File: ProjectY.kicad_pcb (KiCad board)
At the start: 4 copper layers, 100 x 85 mm, 238 parts, among them J15 009155002852006, J16 009155002852006, J17 Out, J2 Conn_ARM_JTAG_SWD_10, J3 9V, J5 IN_R, J6 IN_L, J7 Out, J9 USB_C_Receptacle_USB2.0_14P, Q2 AO3401A, U1 W9825G6KH-6, U11 RT8293B, U12 USBLC6-2P6, U13 LM74700, U14 OPA1678, U2 W25Q128JVS, U201 OPA1678, U202 OPA1678, U203 OPA1678, U204 OPA1678, U205 TAC5242, U206 OPA1678, U3 FM24CL64B, U4 TPS7A39, U5 TL431DBZ, U6 MIMXRT1176CVM8A, U8 TLV77325PDBVR, U9 TL431DBZ, Y1 ASDLJ-E-24.576MHZ-L-R-T, Y3 SG-5032CAN 24MHz

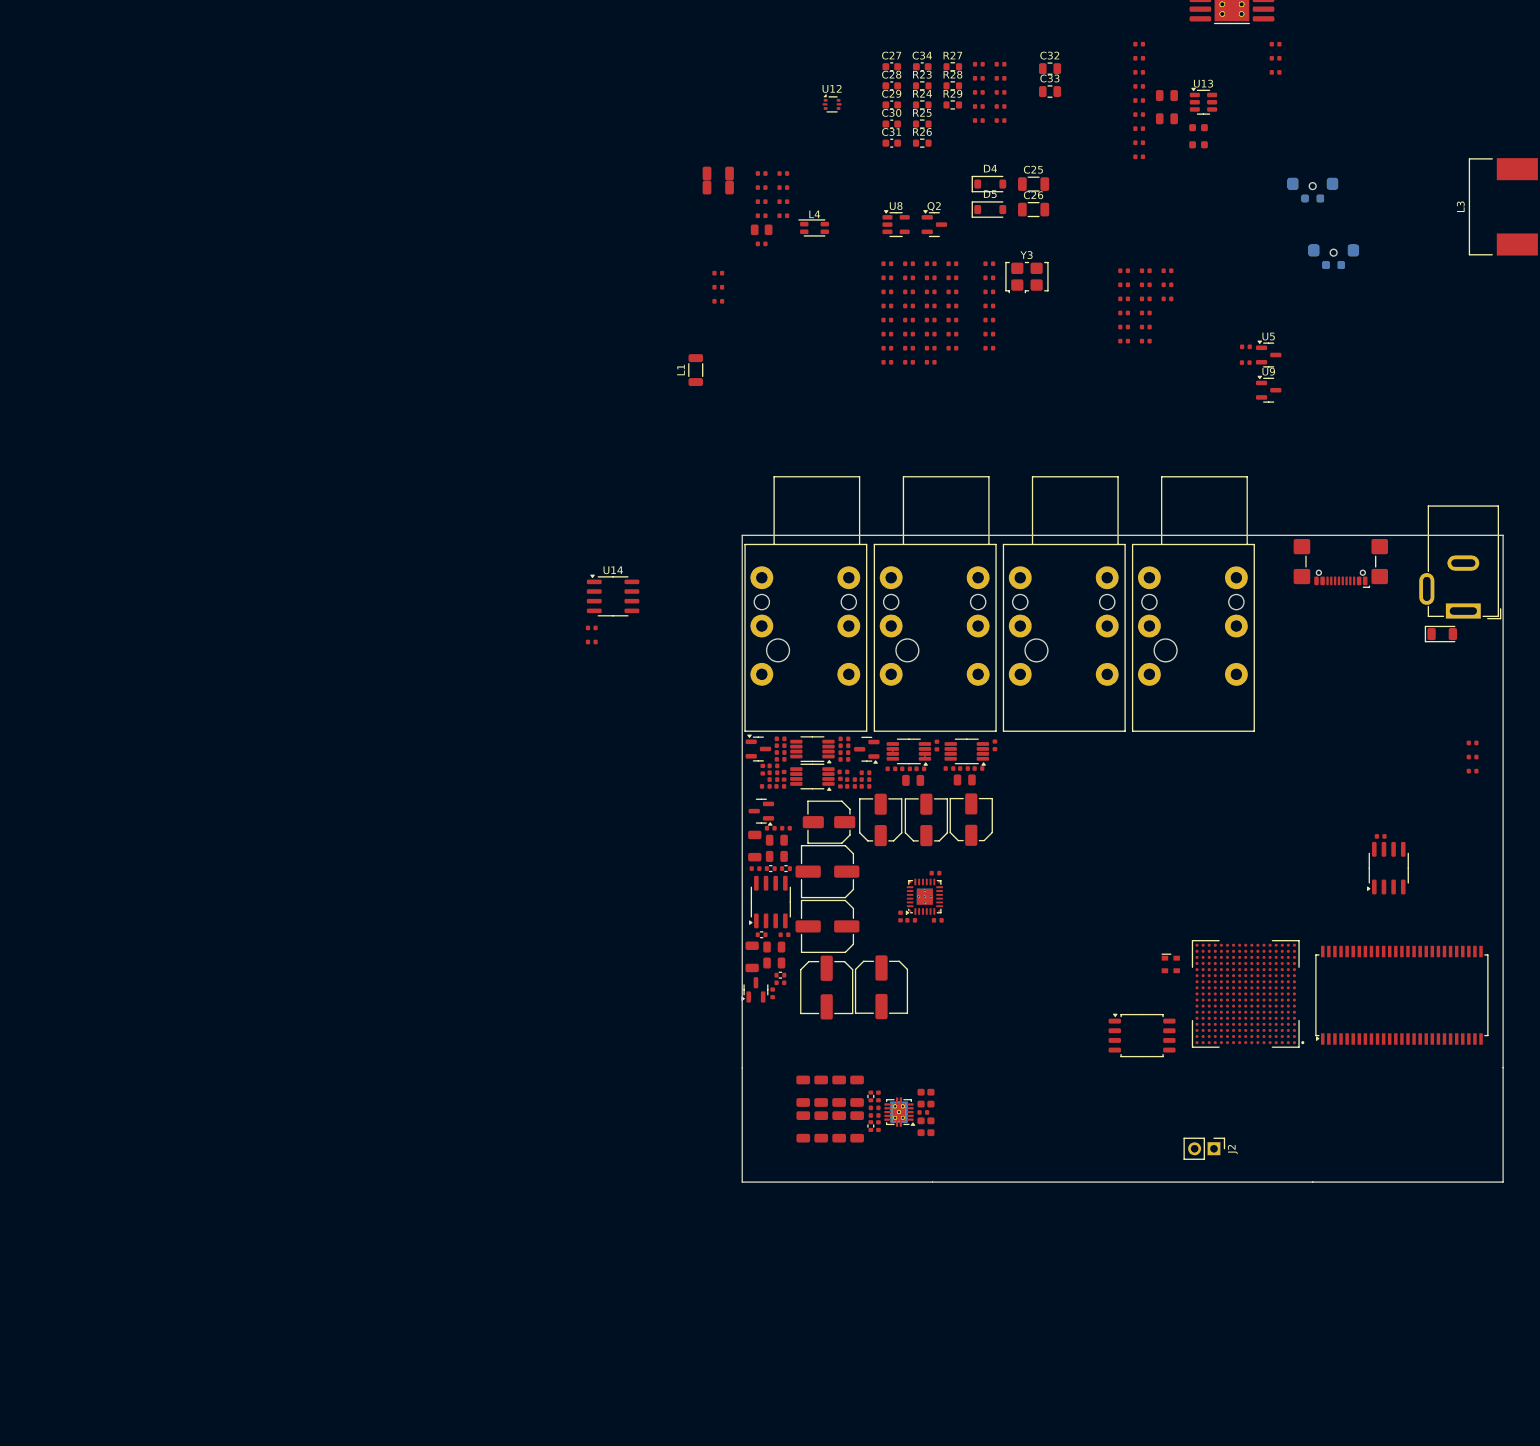
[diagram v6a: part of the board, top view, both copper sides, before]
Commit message: added renesas RA8P1
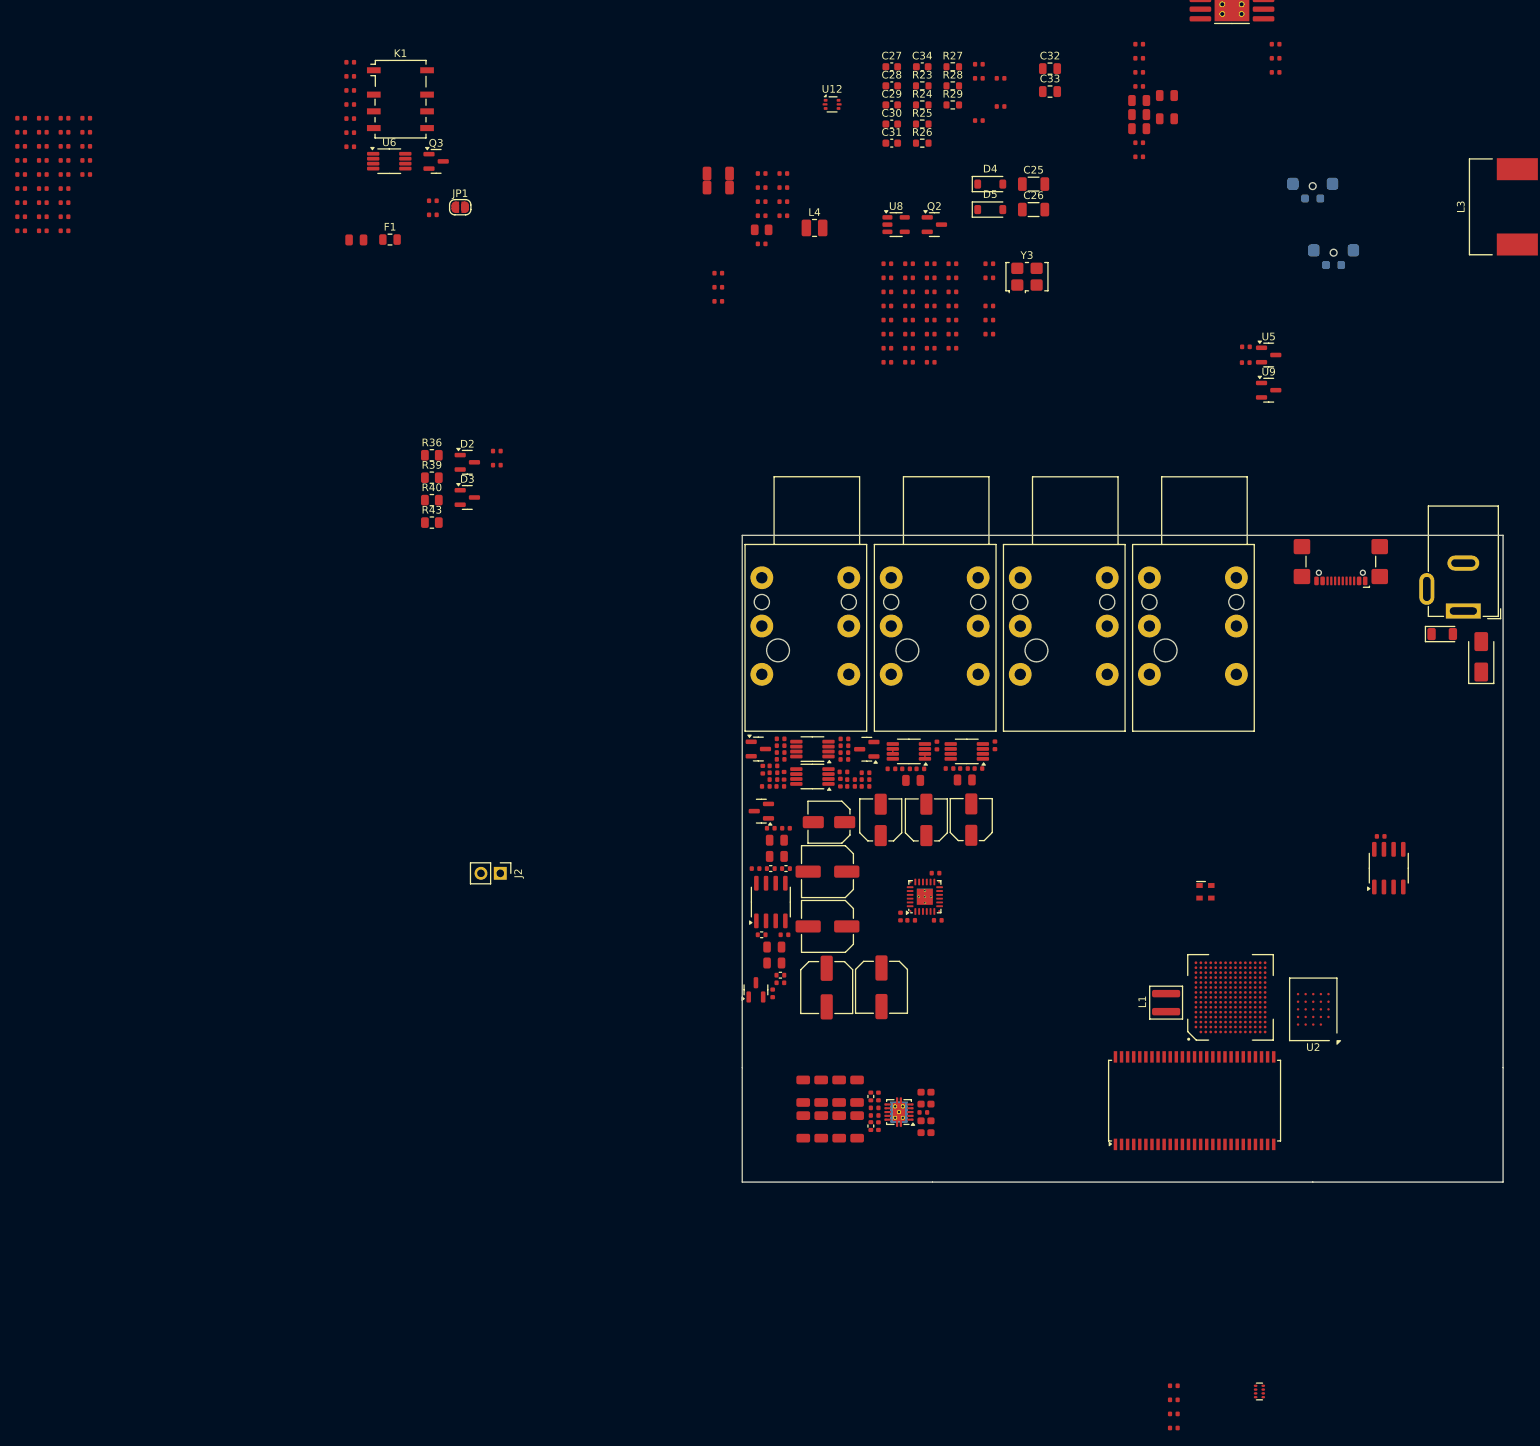
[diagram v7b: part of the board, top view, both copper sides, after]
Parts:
- removed C53, C56: 100nF, PCM_JLCPCB:C_0603
- removed R117: 10kΩ, PCM_JLCPCB:R_0402
- removed R229, R230: 1kΩ, PCM_JLCPCB:R_1206
- removed U13: LM74700, Package_TO_SOT_SMD:SOT-23-6
- removed U14: OPA1678, Package_SO:SOIC-8_3.9x4.9mm_P1.27mm
- added C50: 100pF, PCM_JLCPCB:C_0402, F.Cu at (110.6, 83.8)
- added C60: 4.7uF, PCM_JLCPCB:C_0402, F.Cu at (53.8, 45.6)
- added C63: 100pF, PCM_JLCPCB:C_0402, F.Cu at (110.6, 85.7)
- added C64: 4.7uF, PCM_JLCPCB:C_0402, F.Cu at (53.8, 47.5)
- added C65: 4.7uF, PCM_JLCPCB:C_0402, F.Cu at (53.8, 49.3)
- added C68: 4.7uF, PCM_JLCPCB:C_0402, F.Cu at (53.8, 51.2)
- added C69: 4.7uF, PCM_JLCPCB:C_0402, F.Cu at (53.8, 53.0)
- added C70: 4.7uF, PCM_JLCPCB:C_0402, F.Cu at (53.8, 54.9)
- added C71: 4.7uF, PCM_JLCPCB:C_0402, F.Cu at (56.7, 40.1)
- added C72: 4.7uF, PCM_JLCPCB:C_0402, F.Cu at (56.7, 41.9)
- added C73: 4.7uF, PCM_JLCPCB:C_0402, F.Cu at (56.7, 43.8)
- added C74: 4.7uF, PCM_JLCPCB:C_0402, F.Cu at (56.7, 45.6)
- added C75: 4.7uF, PCM_JLCPCB:C_0402, F.Cu at (56.7, 47.5)
- added C76: 4.7uF, PCM_JLCPCB:C_0402, F.Cu at (199.6, 206.7)
- added C77: 4.7uF, PCM_JLCPCB:C_0402, F.Cu at (199.6, 208.5)
- added C78: 4.7uF, PCM_JLCPCB:C_0402, F.Cu at (199.6, 210.4)
- added C80: 4.7uF, PCM_JLCPCB:C_0402, F.Cu at (199.6, 212.2)
- added C81: 10uF, PCM_JLCPCB:C_0805, F.Cu at (92.2, 56.1)
- added D2: BAV99, Package_TO_SOT_SMD:SOT-23, F.Cu at (106.8, 85.3)
- added D3: BAV99, Package_TO_SOT_SMD:SOT-23, F.Cu at (106.8, 89.9)
- added D6: SS14, PCM_JLCPCB:D_SMA, F.Cu at (240.0, 110.9)
- added F1: 1A, Fuse:Fuse_0805_2012Metric, F.Cu at (96.6, 56.0)
- added IC2: R7KA8P1KFLCAB#UC0, User:BGA-225_15x15_11.0x11.0mm, F.Cu at (207.1, 155.6)
- added JP1: BOOT_Sel, Jumper:SolderJumper-2_P1.3mm_Open_RoundedPad1.0x1.5mm, F.Cu at (105.8, 51.8)
- added K1: G6K-2, Relay_SMD:Relay_DPDT_Omron_G6K-2F-Y, F.Cu at (98.0, 37.6)
- added Q3: BC846, Package_TO_SOT_SMD:SOT-23, F.Cu at (102.7, 45.8)
- added R32: 3.3kΩ, PCM_JLCPCB:R_0402, F.Cu at (91.4, 40.1)
- added R33: 3.3kΩ, PCM_JLCPCB:R_0402, F.Cu at (91.4, 42.0)
- added R34: 1.5kΩ, PCM_JLCPCB:R_0402, F.Cu at (102.2, 52.8)
- added R35: 10kΩ, PCM_JLCPCB:R_0402, F.Cu at (91.4, 43.8)
- added R36: 100,0.1%, Resistor_SMD:R_0805_2012Metric, F.Cu at (102.1, 84.4)
- added R39: 100,0.1%, Resistor_SMD:R_0805_2012Metric, F.Cu at (102.1, 87.3)
- added R40: 100,0.1%, Resistor_SMD:R_0805_2012Metric, F.Cu at (102.1, 90.3)
- added R43: 100,0.1%, Resistor_SMD:R_0805_2012Metric, F.Cu at (102.1, 93.2)
- added R55: 10kΩ, PCM_JLCPCB:R_0402x4, F.Cu at (210.9, 207.4)
- C1, C2, C24, C35, C36, C37, C38, C39, C44, C5, C6, C7, C9: value 10uF -> 4.7uF
- C11: value 220nF -> 4.7uF
- C23, C48, C49: footprint PCM_JLCPCB:C_0402 -> PCM_JLCPCB:C_0805
- C40, C42, C43, C45, C47: value 2.2uF -> 4.7uF
- C46, C67, C8: value 100nF -> 4.7uF
- L1: footprint Inductor_SMD:L_1206_3216Metric -> Inductor_SMD:L_Wuerth_MAPI-4030
- L3: value 3.5u -> 4.7uf
- L4: value L -> 1uH; footprint Inductor_SMD:L_CommonMode_Wurth_WE-CNSW-1206 -> Inductor_SMD:L_1008_2520Metric
- R17: value 33kΩ -> 3.3kΩ
- R22: value 1MΩ -> 3.3kΩ
- R31: value 1MΩ -> 10kΩ
- R7, R9: value 4.7kΩ -> 3.3kΩ
- U2: value W25Q128JVS -> IS25LX512M-JHLE; footprint Package_SO:SOIC-8_5.3x5.3mm_P1.27mm -> Package_BGA:BGA-24_6x8mm_Layout5x5_P1.0mm
- U6: value MIMXRT1176CVM8A -> OPA1678; footprint User:BGA289C80P17X17_1400X1400X152 -> Package_SO:VSSOP-8_3x3mm_P0.65mm
- moved C5 207.7 mm to (48.1, 43.8)
- moved C1 207.7 mm to (48.1, 40.1)
- moved C2 207.7 mm to (48.1, 41.9)
- moved U6 157.0 mm to (96.5, 45.7), turned to 0 degrees
- moved C44 146.3 mm to (53.8, 40.1)
- moved C45 146.3 mm to (53.8, 41.9)
- moved C47 146.3 mm to (53.8, 43.8)
- moved C38 145.7 mm to (51.0, 45.6)
- moved C39 145.7 mm to (51.0, 47.5)
- moved C40 145.7 mm to (51.0, 49.3)
- moved C41 145.7 mm to (51.0, 51.2)
- moved C42 145.7 mm to (51.0, 53.0)
- moved C43 145.7 mm to (51.0, 54.9)
- moved C6 145.7 mm to (48.1, 45.6)
- moved C9 145.4 mm to (48.1, 51.2)
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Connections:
- net /Analog Audio/Line_Output_L renamed /Analog Audio/Line_Output_L+
- net /Analog Audio/Line_Output_R renamed /Analog Audio/Line_Output_R+
- net Net-(R211-Pad2) renamed /Analog Audio/Analog_Dry_In_R
- net Net-(R212-Pad2) renamed /Analog Audio/Analog_Dry_In_L
- net Net-(U205-AVDD) renamed /Analog Audio/3.3V_AVDD
- C11 pad 1: Net-(U6A-DCDC_PSWITCH) -> +3.3V
- C231 pad 1: DAC_R+ -> DAC_R-
- C232 pad 1: DAC_R- -> DAC_R+
- C234 pad 1: Net-(U14B-+) -> Net-(U6B-+)
- C234 pad 2: Net-(U14B--) -> Net-(U6B--)
- C237 pad 1: Net-(U14B-+) -> Net-(U6B-+)
- C237 pad 2: Net-(U14B--) -> Net-(U6B--)
- C238 pad 1: Net-(U14A-+) -> Net-(U6A-+)
- C238 pad 2: Net-(U14A--) -> Net-(U6A--)
- C24 pad 1: 1.15V_DCDC -> +3.3V
- C240 pad 1: Net-(U14A-+) -> Net-(U6A-+)
- C240 pad 2: Net-(U14A--) -> Net-(U6A--)
- C35 pad 1: 1.15V_DCDC -> +3.3V
- C36 pad 1: 1.15V_DCDC -> +3.3V
- C37 pad 1: 1.15V_DCDC -> +3.3V
- C38 pad 1: 1.15V_DCDC -> +3.3V
- C39 pad 1: 1.15V_DCDC -> +3.3V
- C40 pad 1: /PSU/VDD_LPSR_ANA -> +3.3V
- C402 pad 1: +9VA -> +7V
- C404 pad 1: +9VA -> +7V
- C41 pad 1: /PSU/VDD_LPSR_DIG -> +3.3V
- C42 pad 1: /PSU/VDDA_1P0 -> +3.3V
- C43 pad 1: /PSU/VDDA_1P0 -> +3.3V
- C45 pad 1: /PSU/VDD_SNVS_ANA -> +3.3V
- C47 pad 1: /PSU/VDD_SNVS_ANA -> Net-(IC2A-VCL0)
- C6 pad 1: 1.8V_DCDC -> +3.3V
- C8 pad 1: /PSU/DCDC_MODE -> +3.3V
- C9 pad 1: 1.8V_DCDC -> +3.3V
- D1 pad 1: +9VA -> Net-(D1-Pad1)
- J17 pad R: unconnected-(J17-PadR) -> /Analog Audio/Line_Output_R-
- J2 pad 1: /DSP/VTREF -> +3.3V
- J3 pad 2: +9VA -> Net-(D1-Pad1)
- J5 pad TN: /Analog Audio/IN_L -> GND
- J7 pad R: unconnected-(J7-PadR) -> /Analog Audio/Line_Output_L-
- L1 pad 1: Net-(L1-Pad1) -> Net-(IC2A-VCL0)
- L1 pad 2: Net-(L1-Pad2) -> Net-(IC2A-VLO_1)
- R14 pad 1: +3.3V -> /DSP/FRAM_SCL
- R14 pad 2: /DSP/FRAM_SDA -> +3.3V
- R16 pad 2: /DSP/FRAM_SCL -> /DSP/FRAM_SDA
- R17 pad 1: +3.3V -> Net-(K1-Pad6)
- R17 pad 2: Net-(U6A-DCDC_PSWITCH) -> /Analog Audio/Summing_Amp_In_R
- R203 pad 2: Net-(R203-Pad2) -> GND
- R204 pad 2: Net-(R204-Pad2) -> GND
- R22 pad 1: Net-(R204-Pad2) -> /Analog Audio/Effect_Signal_R
- R22 pad 2: GND -> /Analog Audio/Summing_Amp_In_R
- R221 pad 2: Net-(U14B--) -> Net-(U6B--)
- R222 pad 2: Net-(U14B-+) -> Net-(U6B-+)
- R223 pad 2: Net-(U14B-+) -> Net-(U6B-+)
- R224 pad 2: Net-(U14A--) -> Net-(U6A--)
- R225 pad 2: Net-(U14A-+) -> Net-(U6A-+)
- R226 pad 2: Net-(U14A-+) -> Net-(U6A-+)
- R227 pad 1: Net-(U14B--) -> Net-(U6B--)
- R227 pad 2: Net-(R227-Pad2) -> /Analog Audio/Effect_Signal_R
- R228 pad 1: Net-(U14A--) -> Net-(U6A--)
- R228 pad 2: Net-(R228-Pad2) -> /Analog Audio/Effect_Signal_L
- R31 pad 1: Net-(R203-Pad2) -> +3.3V
- R31 pad 2: GND -> /DSP/BOOT_MODE
- R7 pad 1: /PSU/DCDC_MODE -> /Analog Audio/Summing_Amp_In_L
- R7 pad 2: GND -> Net-(R40-Pad1)
- R9 pad 1: /DSP/JTAG_MOD -> /Analog Audio/Summing_Amp_In_R
- R9 pad 2: GND -> Net-(R36-Pad1)
- U206 pad 1: unconnected-(U206-Pad1) -> Net-(R40-Pad1)
- U206 pad 2: unconnected-(U206A---Pad2) -> /Analog Audio/Summing_Amp_In_L
- U206 pad 3: unconnected-(U206A-+-Pad3) -> GND
- U206 pad 5: unconnected-(U206B-+-Pad5) -> GND
- U206 pad 6: unconnected-(U206B---Pad6) -> /Analog Audio/Summing_Amp_In_R
- U206 pad 7: unconnected-(U206-Pad7) -> Net-(R36-Pad1)
- U4 pad 1: +9VA -> +7V
- U4 pad 2: +9VA -> +7V
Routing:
- added copper zone on In1.Cu, net GND
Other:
- copper layers 4 -> 6
